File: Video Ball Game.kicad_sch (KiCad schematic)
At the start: 171 parts, among them J1 RIGHT CONTROL, J10 GND, J11 GND, J12 D, J13 BL, J14 CL, J15 Video, J16 BR, J17 USB_B_Micro, J2 LEFT CONTROL, J3 FS, J4 UL, J5 NH, J6 LL, J7 GND, J8 LS, J9 GND, U1 4011 QUAD NAND, U10 4011 QUAD NAND, U11 4001 QUAD NOR, U12 4001 QUAD NOR, U13 4001 QUAD NOR, U14 L7806, U2 4011 QUAD NAND, U3 4011 QUAD NAND, U4 4011 QUAD NAND, U5 4001 QUAD NOR, U6 4001 QUAD NOR, U7 4001 QUAD NOR, U8 4001 QUAD NOR, U9 4011 QUAD NAND

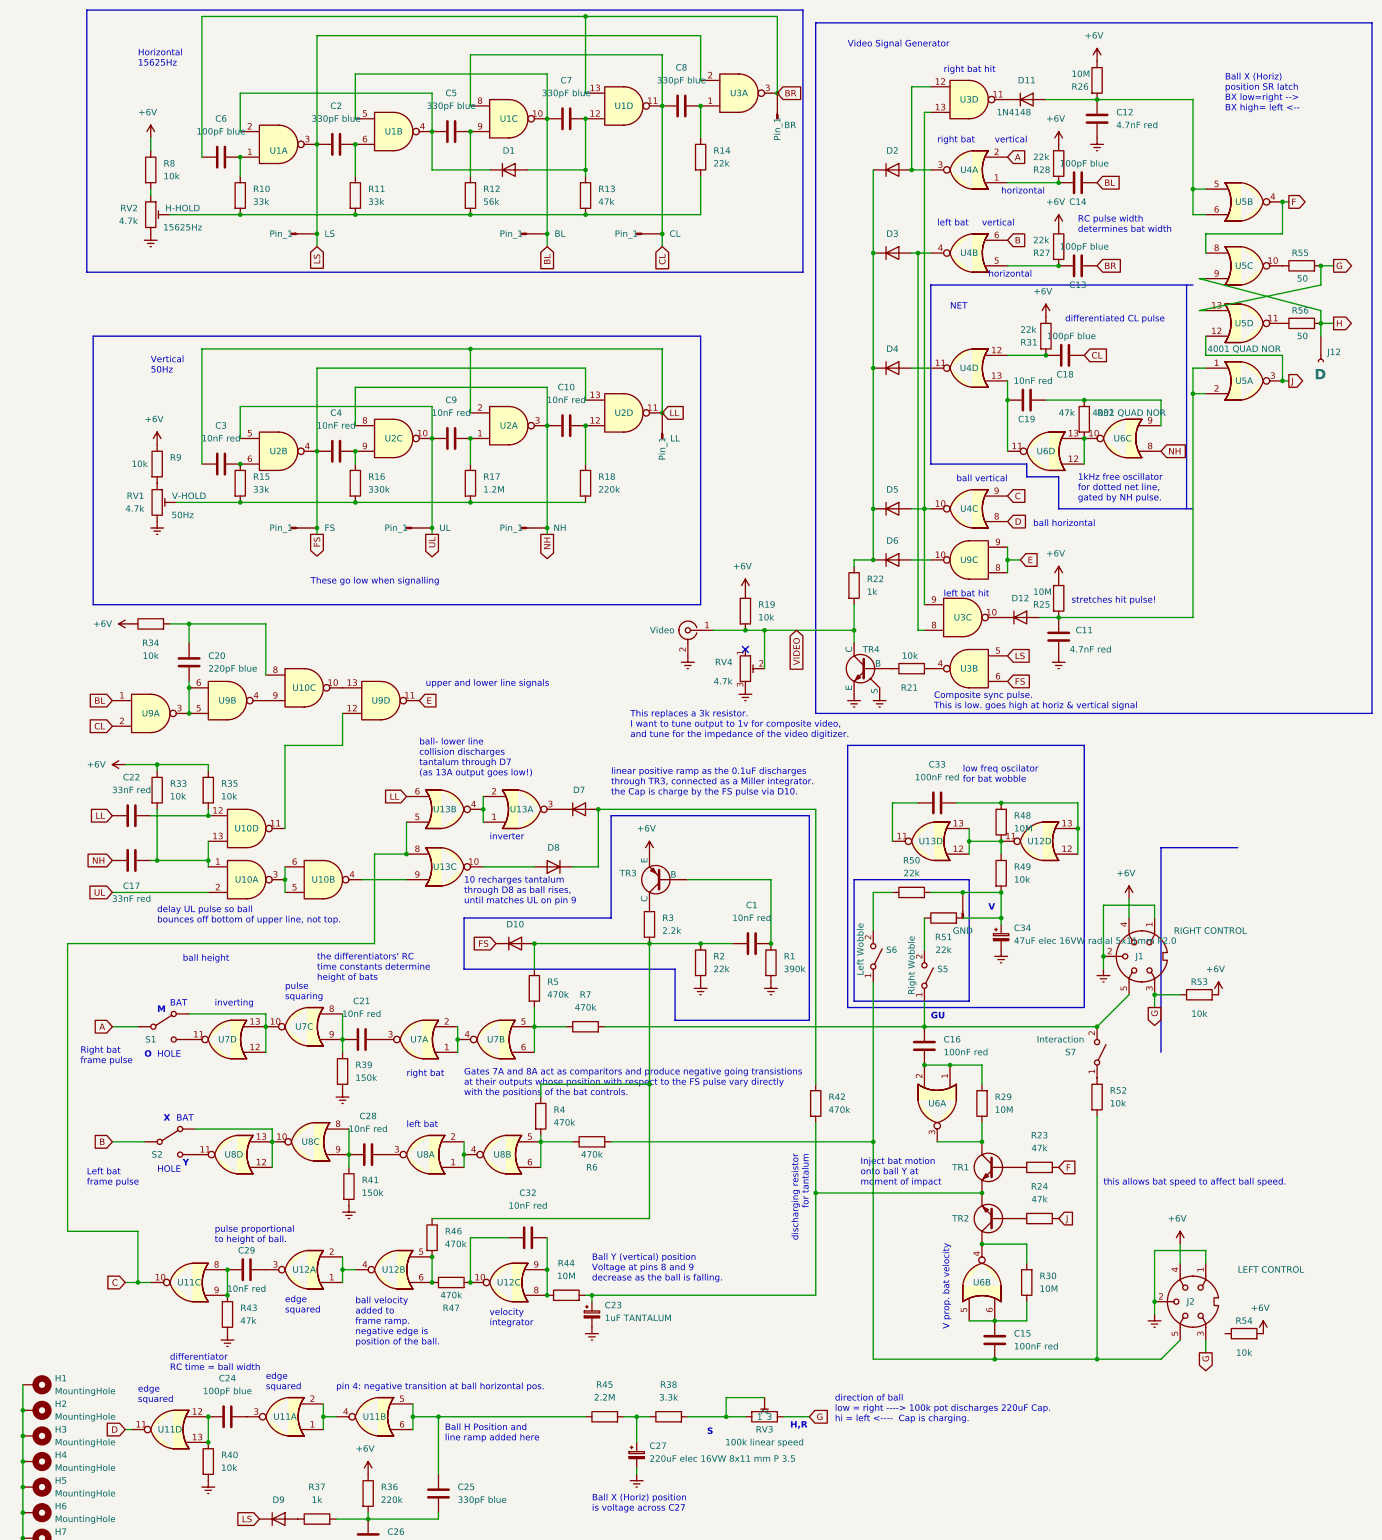
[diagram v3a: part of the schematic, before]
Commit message: updated to Kicad 9.0
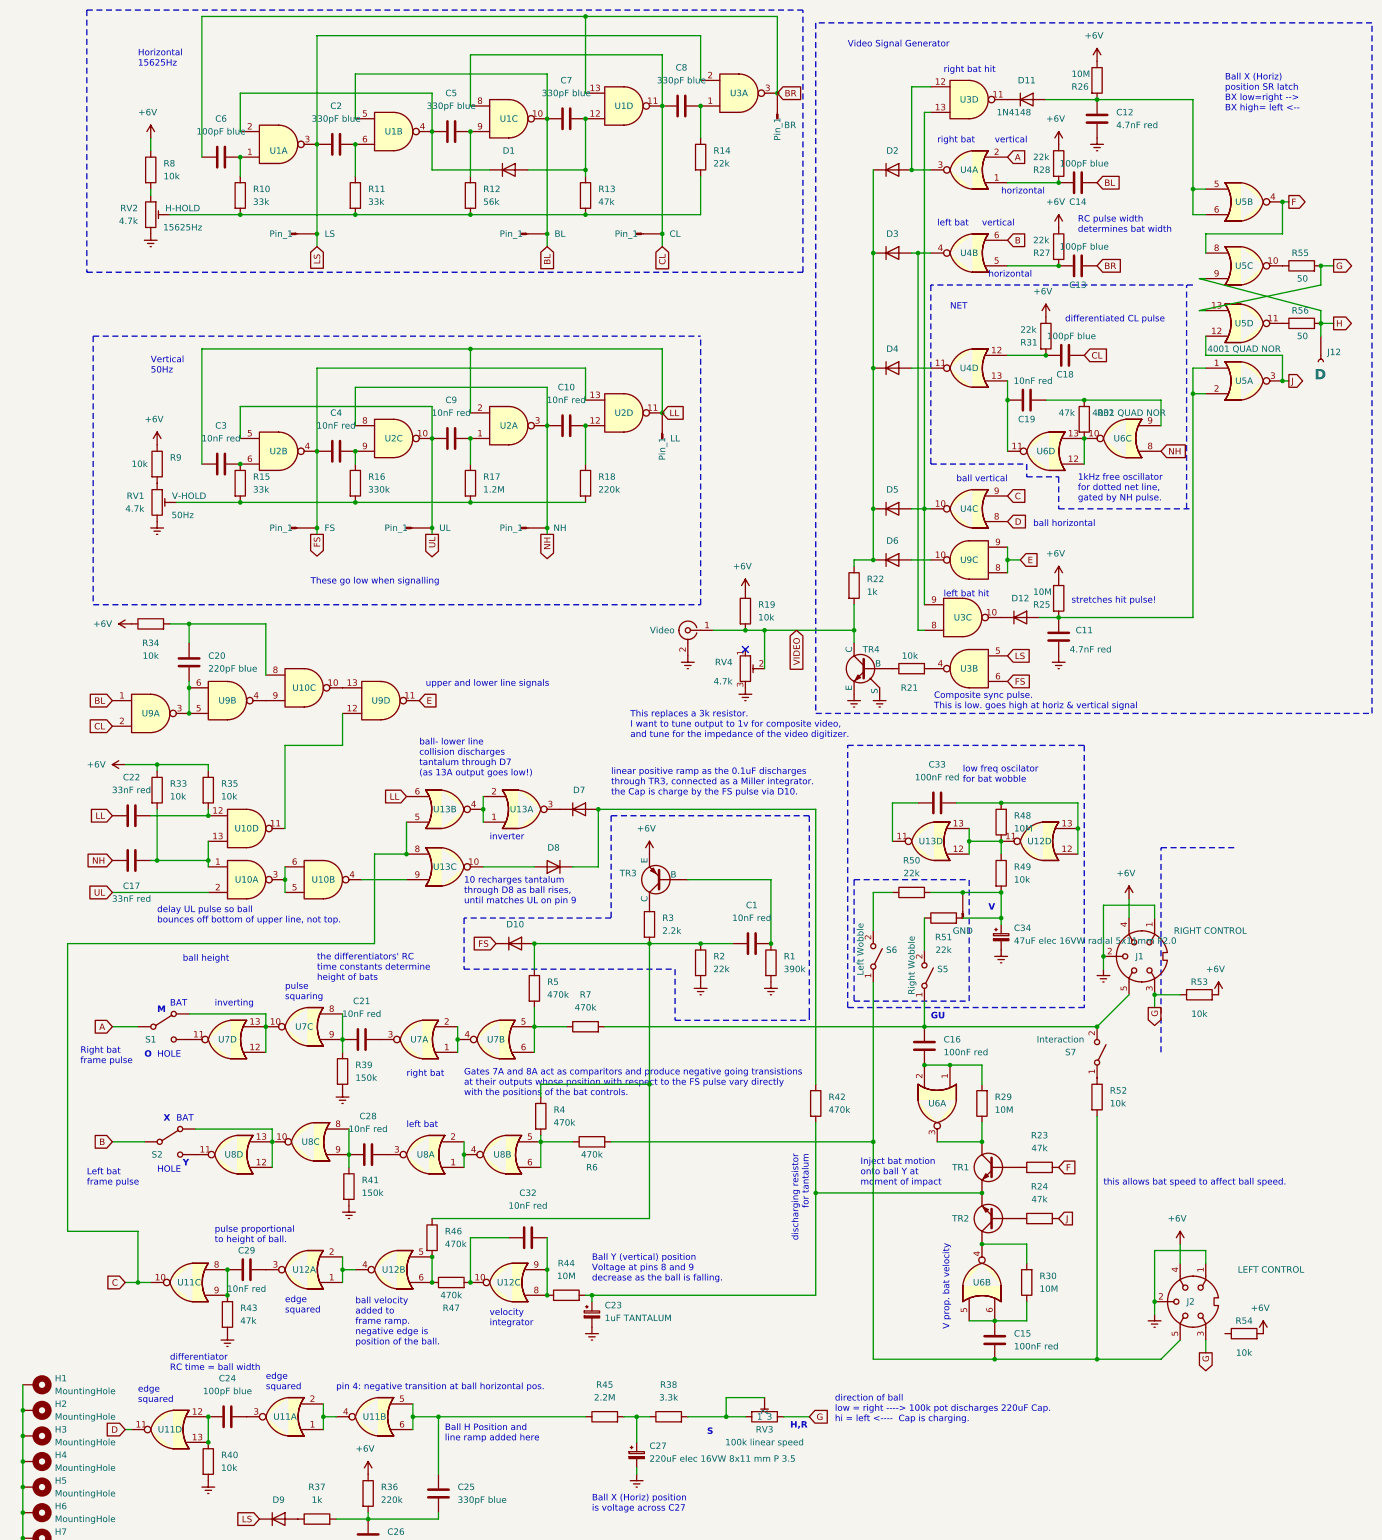
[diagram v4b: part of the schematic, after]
